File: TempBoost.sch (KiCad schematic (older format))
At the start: 48 parts, among them J1 Conn_01x02, J2 Conn_01x02, Q201 Q_NMOS_GSD, SW101 SW_SPST, T101 3FD-224, U101 DF005S2, U201 MIC2920, U203 UCC27517A, U204 2925, U205 LM1117-5.0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

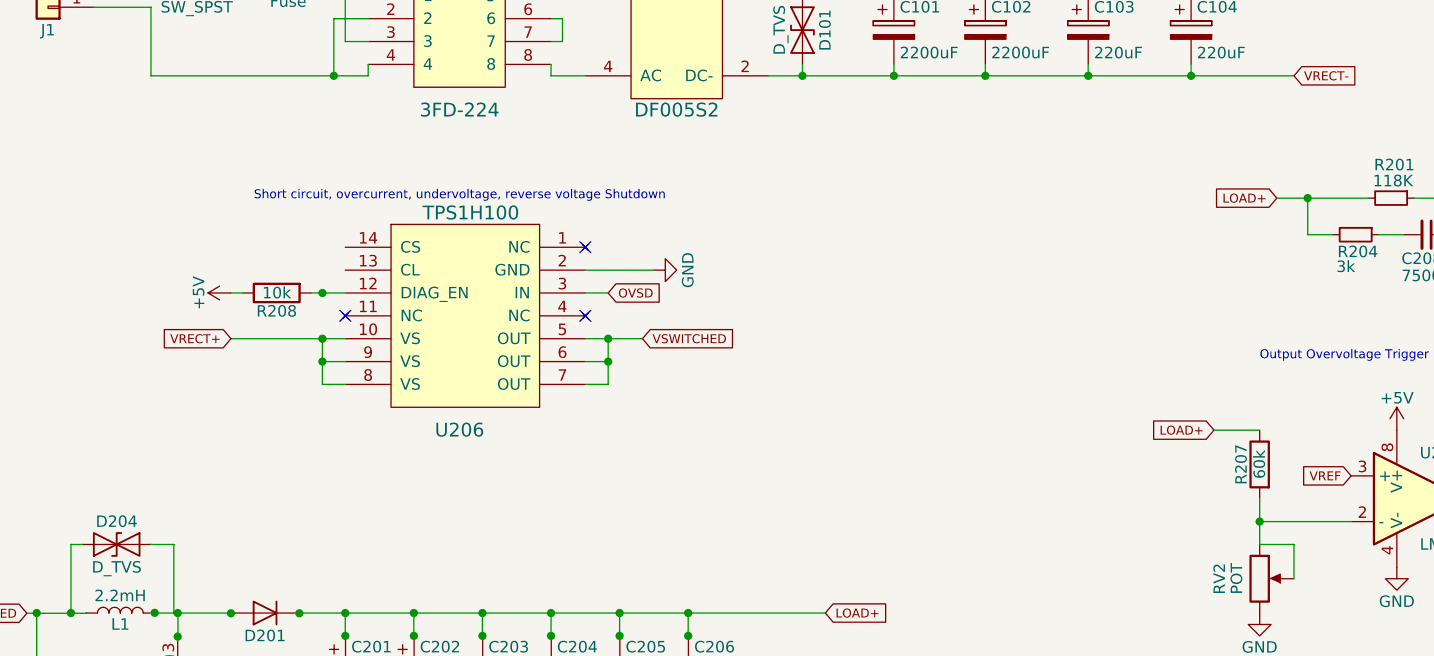
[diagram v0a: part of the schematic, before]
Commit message: Need to add back in the PWM
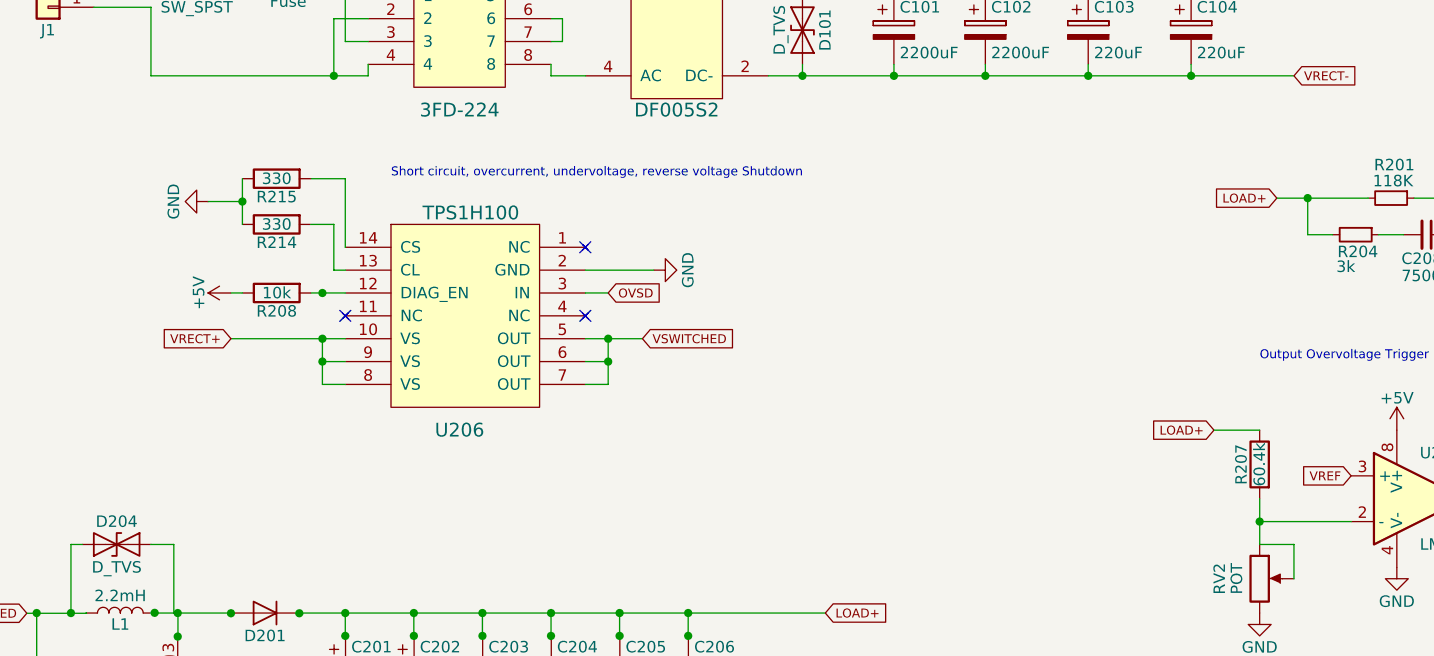
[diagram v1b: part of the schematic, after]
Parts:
- added R214, R215: 330, Resistors_SMD:R_0805, symbol R
- R207: value 60k -> 60.4k
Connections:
- wire segments 133 -> 140
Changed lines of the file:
@@
 P 6500 3200
 F 0 "R207" V 6580 3200 50  0000 C CNN
-F 1 "60k" V 6500 3200 50  0000 C CNN
+F 1 "60.4k" V 6500 3200 50  0000 C CNN
 F 2 "Resistors_SMD:R_0805" V 6430 3200 50  0001 C CNN
 F 3 "" H 6500 3200 50  0001 C CNN
@@
 	1    0    0    -1
 $EndComp
-Text Notes 2100 2050 0    39   ~ 0
+Text Notes 2700 1950 0    39   ~ 0
 Short circuit, overcurrent, undervoltage, reverse voltage Shutdown
 Text Notes 6500 2750 0    39   ~ 0
@@
 Connection ~ 8651 2049
 Connection ~ 8557 2034
+$Comp
+L R R214
+U 1 1 5CAD9A73
+P 2200 2150
+F 0 "R214" V 2280 2150 50  0000 C CNN
+F 1 "330" V 2200 2150 50  0000 C CNN
+F 2 "Resistors_SMD:R_0805" V 2130 2150 50  0001 C CNN
+F 3 "" H 2200 2150 50  0001 C CNN
+	1    2200 2150
+	0    -1   1    0
+$EndComp
+$Comp
+L R R215
+U 1 1 5CAD9BCF
+P 2200 1950
+F 0 "R215" V 2280 1950 50  0000 C CNN
+F 1 "330" V 2200 1950 50  0000 C CNN
+F 2 "Resistors_SMD:R_0805" V 2130 1950 50  0001 C CNN
+F 3 "" H 2200 1950 50  0001 C CNN
+	1    2200 1950
+	0    -1   1    0
+$EndComp
+Wire Wire Line
+	2350 1950 2500 1950
+Wire Wire Line
+	2500 1950 2500 2250
+Wire Wire Line
+	2500 2350 2450 2350
+Wire Wire Line
+	2450 2350 2450 2150
+Wire Wire Line
+	2450 2150 2350 2150
+Wire Wire Line
+	2050 1950 2050 2150
+$Comp
+L GND #PWR?
+U 1 1 5CADB4E5
+P 1900 2050
+F 0 "#PWR?" H 1900 1800 50  0001 C CNN
+F 1 "GND" H 1900 1900 50  0000 C CNN
+F 2 "" H 1900 2050 50  0001 C CNN
+F 3 "" H 1900 2050 50  0001 C CNN
+	1    1900 2050
+	0    1    1    0
+$EndComp
+Wire Wire Line
+	1900 2050 2050 2050
+Connection ~ 2050 2050
 $EndSCHEMATC

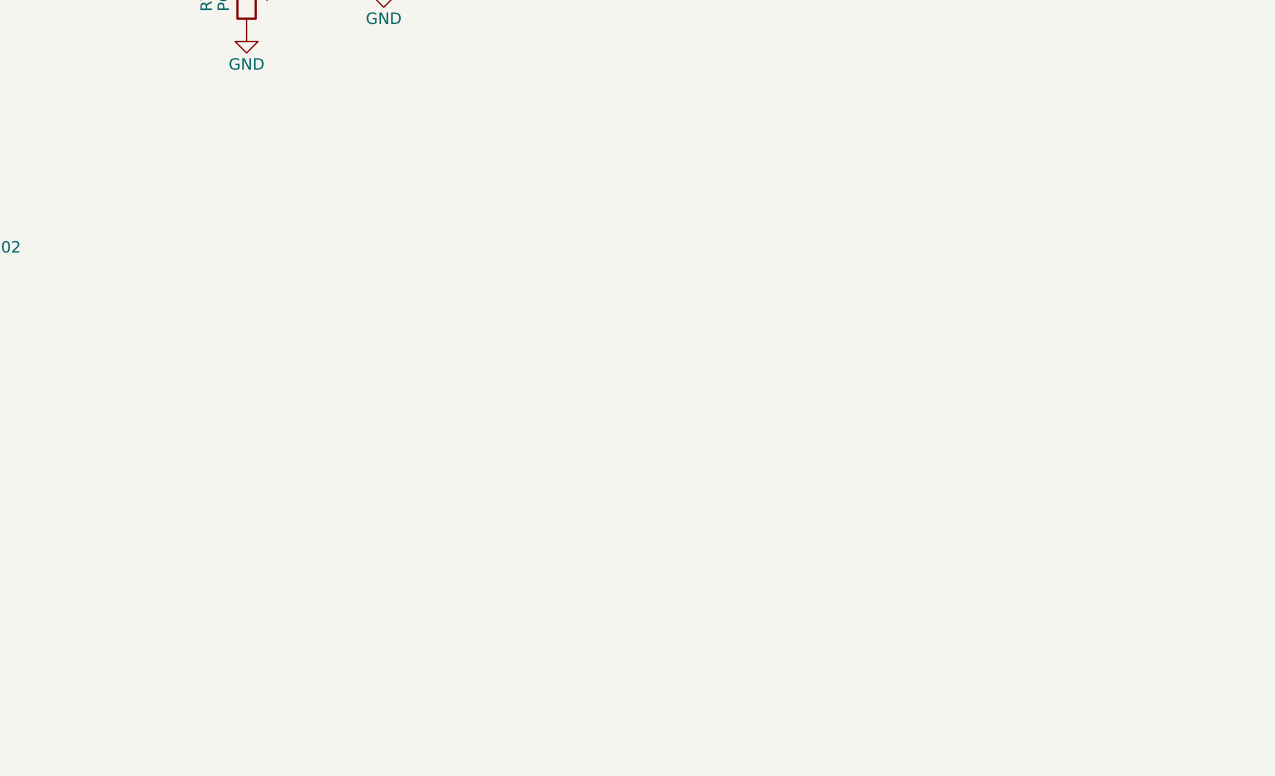
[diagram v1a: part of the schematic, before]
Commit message: Added PWM Gen Library
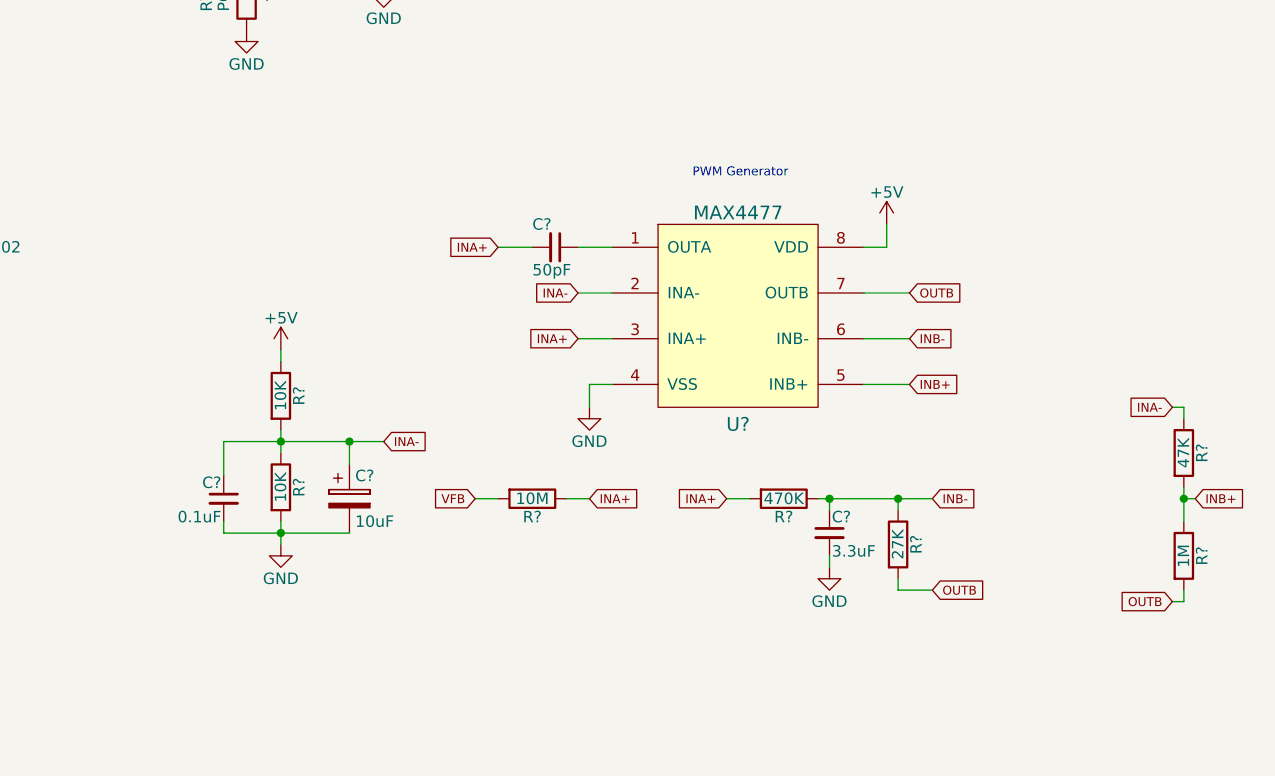
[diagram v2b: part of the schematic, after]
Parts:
- added C?: 50pF, symbol C_Small
- added C?: 3.3uF, symbol C_Small
- added C?: 10uF, symbol CP
- added C?: 0.1uF, symbol C_Small
- added R?: 10M, symbol R
- added R?: 470K, symbol R
- added R?: 27K, symbol R
- added R?: 47K, symbol R
- added R?: 1M, symbol R
- added R? (x2): 10K, symbol R
- added U?: MAX4477, symbol MAX4477
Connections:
- net labels added: INA+, INA-, INB+, INB-, OUTB
- wire segments 140 -> 174
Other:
- note added: "PWM Generator"

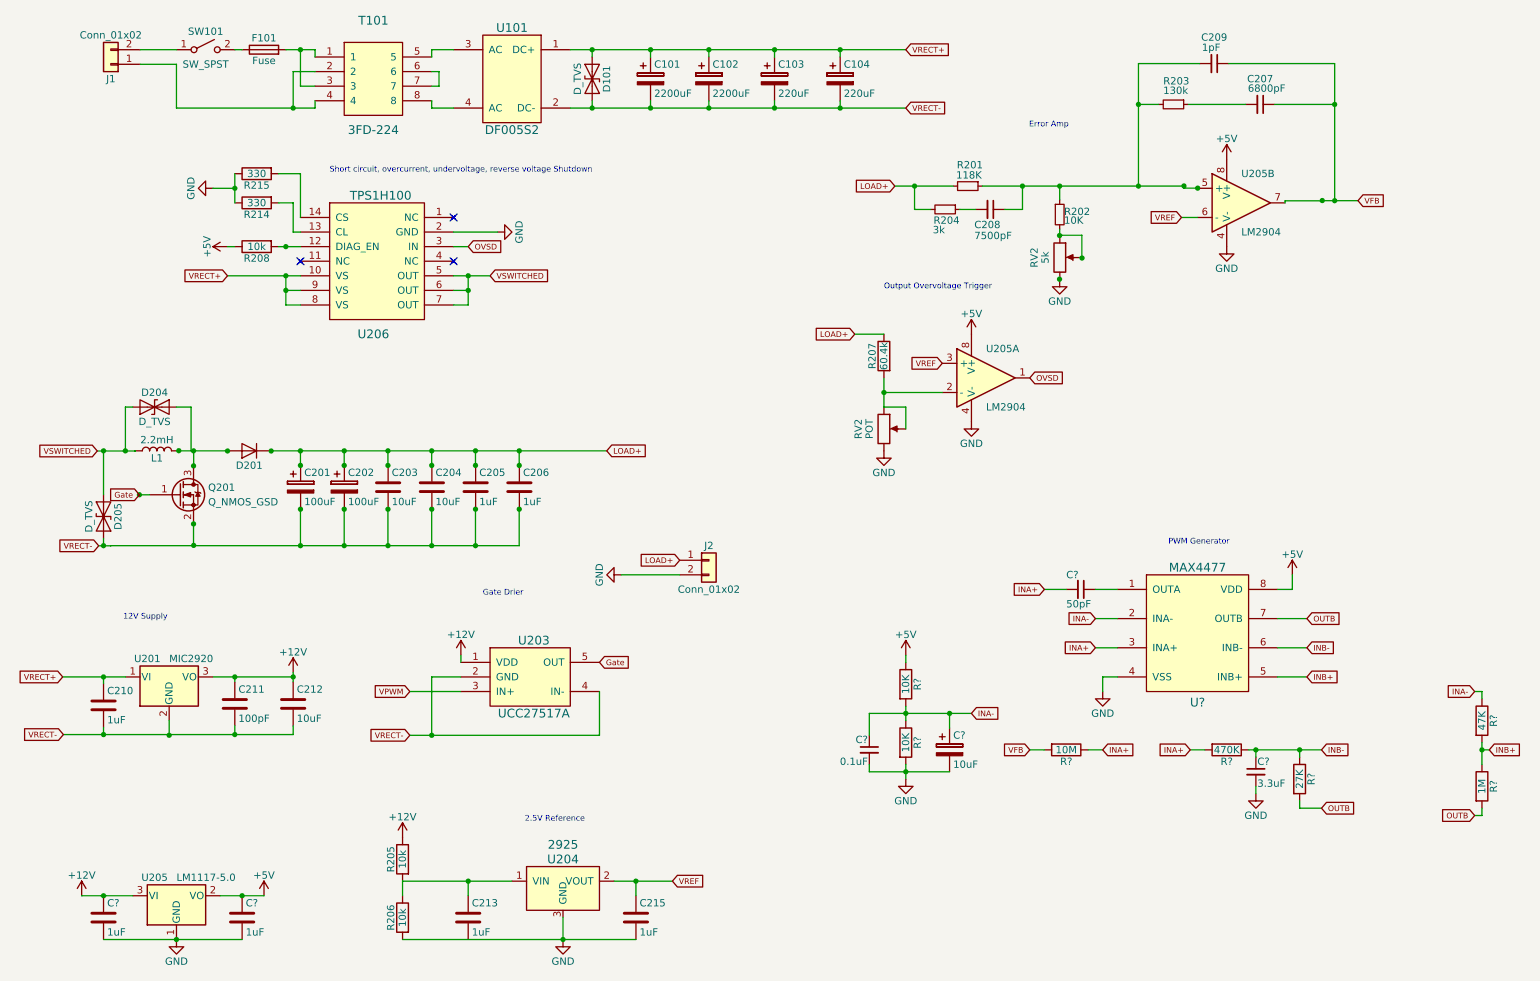
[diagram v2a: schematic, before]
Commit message: Redid Footprint associations
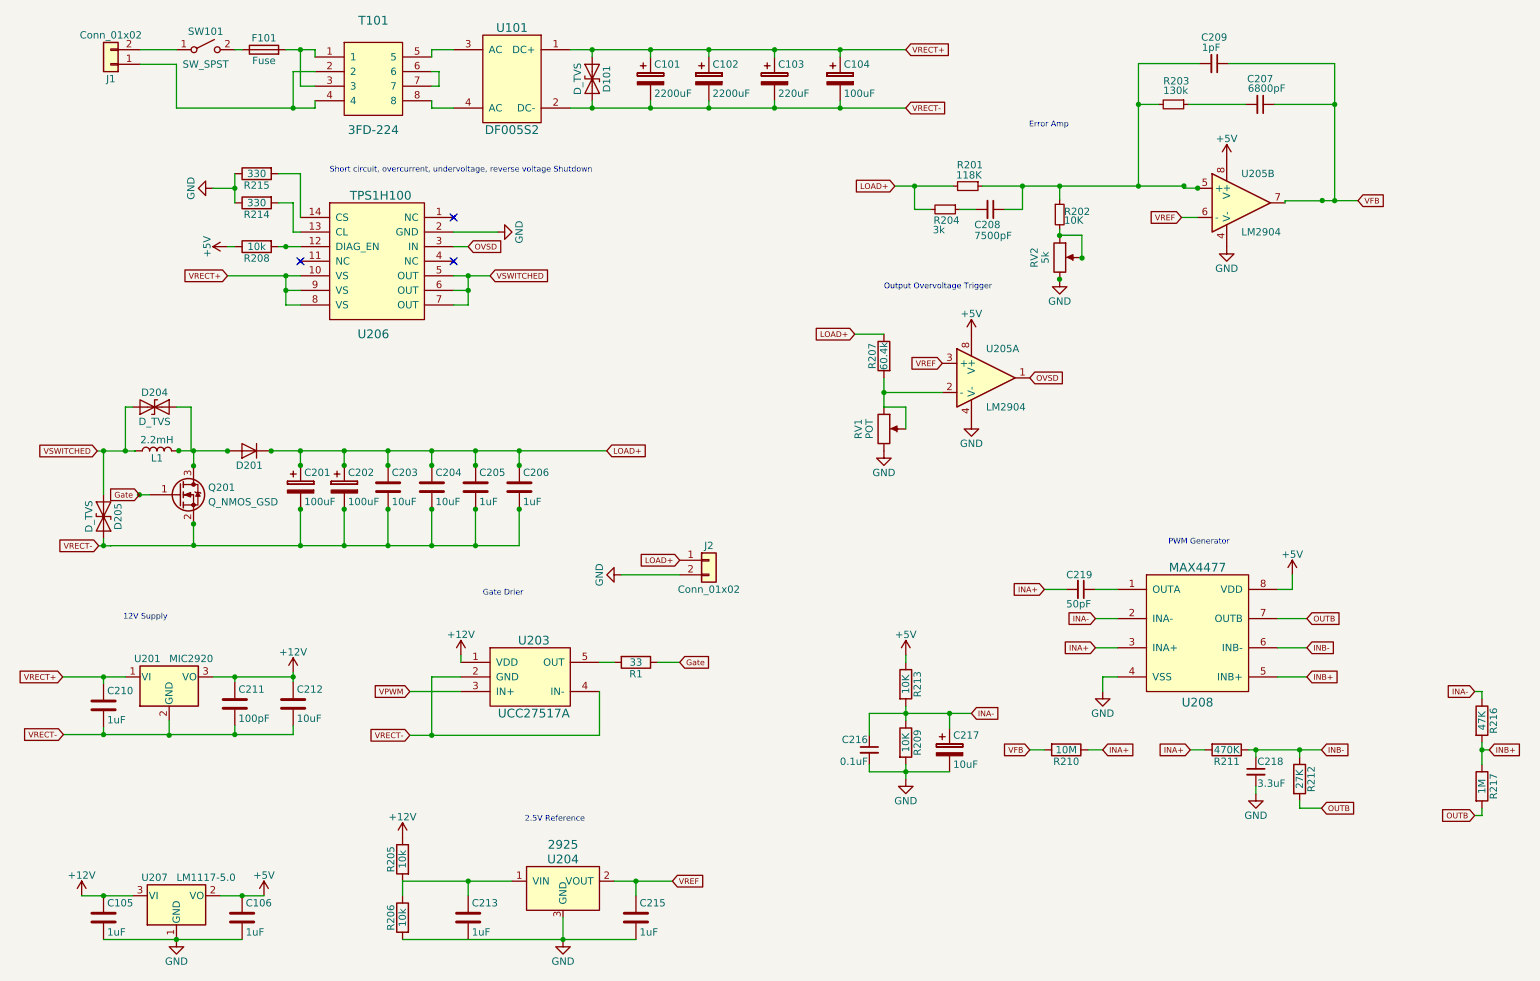
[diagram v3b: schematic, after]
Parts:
- added R1: 33, Resistors_THT:R_Axial_DIN0614_L14.3mm_D5.7mm_P20.32mm_Horizontal, symbol R
- C101, C102: footprint (none) -> BoostLib:CP_Elec_19x19
- C103: footprint (none) -> Capacitors_THT:CP_Radial_D12.5mm_P5.00mm
- C104: value 220uF -> 100uF; footprint (none) -> Capacitors_SMD:CP_Elec_6.3x7.7
- C201, C202: footprint Capacitors_SMD:C_0805 -> Capacitors_SMD:CP_Elec_6.3x7.7
- C207, C208, C209: footprint (none) -> Capacitors_SMD:C_0603
- C216: renamed from C?; footprint (none) -> Capacitors_THT:C_Axial_L5.1mm_D3.1mm_P10.00mm_Horizontal
- C217, C218: renamed from C?; footprint (none) -> Capacitors_THT:C_Disc_D5.0mm_W2.5mm_P2.50mm
- C219: renamed from C?; footprint (none) -> Capacitors_SMD:C_0603
- D101, D204, D205: footprint (none) -> BoostLib:SMAJ40ALFCT
- F101: footprint (none) -> SMD_Packages:SMD-1206_Pol
- J1: footprint (none) -> ED1202DS:ED1202DS
- J2: footprint (none) -> BoostLib:ED120DS
- R201, R202: footprint (none) -> Resistors_SMD:R_0805
- R203, R204: footprint (none) -> Resistors_SMD:R_0603
- R209, R210, R213: renamed from R?; footprint (none) -> Resistors_SMD:R_0805
- R211, R212, R216, R217: renamed from R?; footprint (none) -> Resistors_SMD:R_0603
- RV1: renamed from RV2; footprint (none) -> Potentiometers:Potentiometer_Trimmer_Bourns_3296W
- RV2: footprint (none) -> Potentiometers:Potentiometer_Trimmer_Bourns_3296W
- SW101: footprint (none) -> 400MSP1R6BLKM6QE:400MSP1R6BLKM6QE
- T101: footprint (none) -> 3FD-224:3FD-224
- U101: footprint (none) -> BoostLib:DF10S2
- U203: footprint (none) -> TO_SOT_Packages_SMD:SOT-23-5
- U206: footprint (none) -> Housings_SSOP:TSSOP-14-1EP_4.4x5mm_Pitch0.65mm
- U207: renamed from U205; footprint (none) -> TO_SOT_Packages_SMD:SOT-223-3_TabPin2
- U208: renamed from U?; footprint (none) -> Housings_SOIC:SOIC-8_3.9x4.9mm_Pitch1.27mm
- gave numbers to parts that had none: 2
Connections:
- wire segments 174 -> 176

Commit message: Fixed Half of Netlist
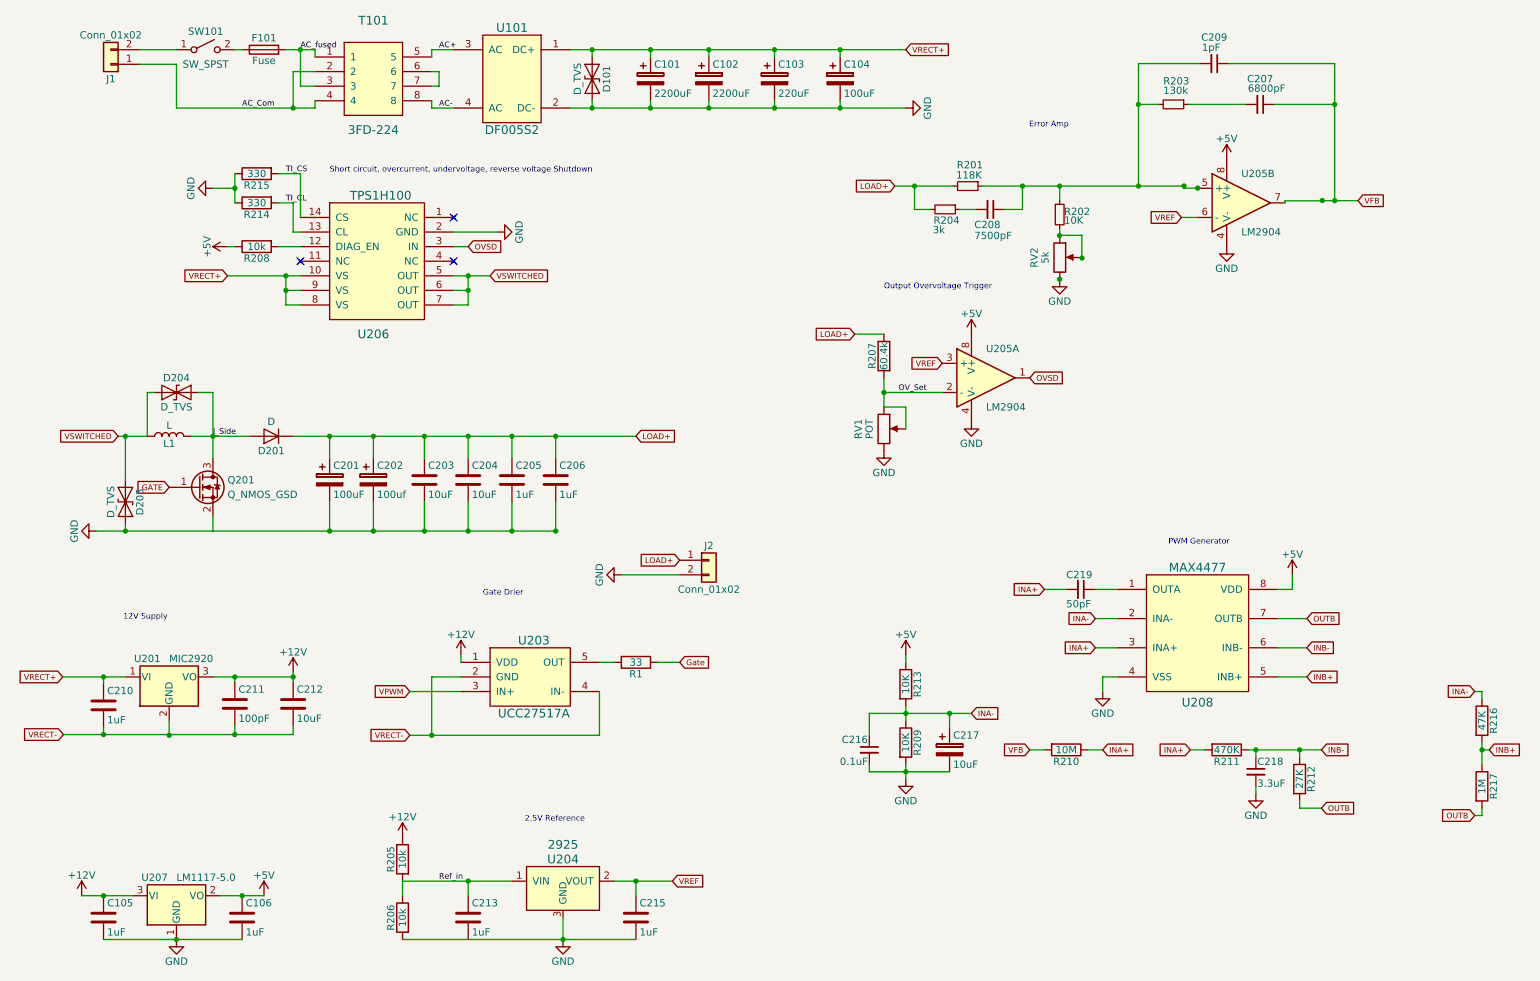
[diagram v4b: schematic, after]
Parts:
- C201: Part Number 1 -> (none)
- C202: value 100uF -> 100uf
- D201: Manufactuer Rohm -> (none); Part Number RFN10BM3SFHTL -> (none)
- J2: footprint BoostLib:ED120DS -> ED1202DS:ED1202DS
- L1: value 2.2mH -> L; Manufactuer Bourns -> (none); Part Number 1140-122K-RC -> (none)
- Q201: Manufactuer Vishay -> (none); Part Number SQ2348ES-T1_GE3 -> (none)
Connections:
- net labels added: AC+, AC-, AC_Com, AC_fused, GATE, I_Side, OV_Set, Ref_in, TI_CL, TI_CS
- wire segments 176 -> 165
